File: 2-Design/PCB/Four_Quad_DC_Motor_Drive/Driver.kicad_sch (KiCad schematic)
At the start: 0 parts

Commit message: Changed the driver schematic, and added some schematic symbols
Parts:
- added C? (x3): 0.1uF, symbol Device:C_Polarized_Small_US
- added Q1, Q2, Q3, Q4: SPW47N60, symbol Device:Q_NMOS_GDS
- added U? (x4): HCPL-3120, Package_DIP:DIP-8_W7.62mm, symbol Driver_FET:HCPL-3120
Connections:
- new net: Q3.1 (G), U?.6 (VO), U?.7 (VO)
- new net: Q1.1 (G), U?.6 (VO), U?.7 (VO)
- new net: Q2.1 (G), U?.6 (VO), U?.7 (VO)
- new net: Q4.1 (G), U?.6 (VO), U?.7 (VO)
- new net +12V: C?.1, C?.1, C?.1, U?.8 (VCC), U?.8 (VCC), U?.8 (VCC), U?.8 (VCC)
- new net HVDC+: Q1.2 (D), Q3.2 (D)
- new net HVDC-: C?.2, Q2.3 (S), Q4.3 (S), U?.5 (VEE), U?.5 (VEE)
- new net MOTOR+: C?.2, Q1.3 (S), Q2.2 (D), U?.5 (VEE)
- new net MOTOR-: C?.2, Q3.3 (S), Q4.2 (D), U?.5 (VEE)

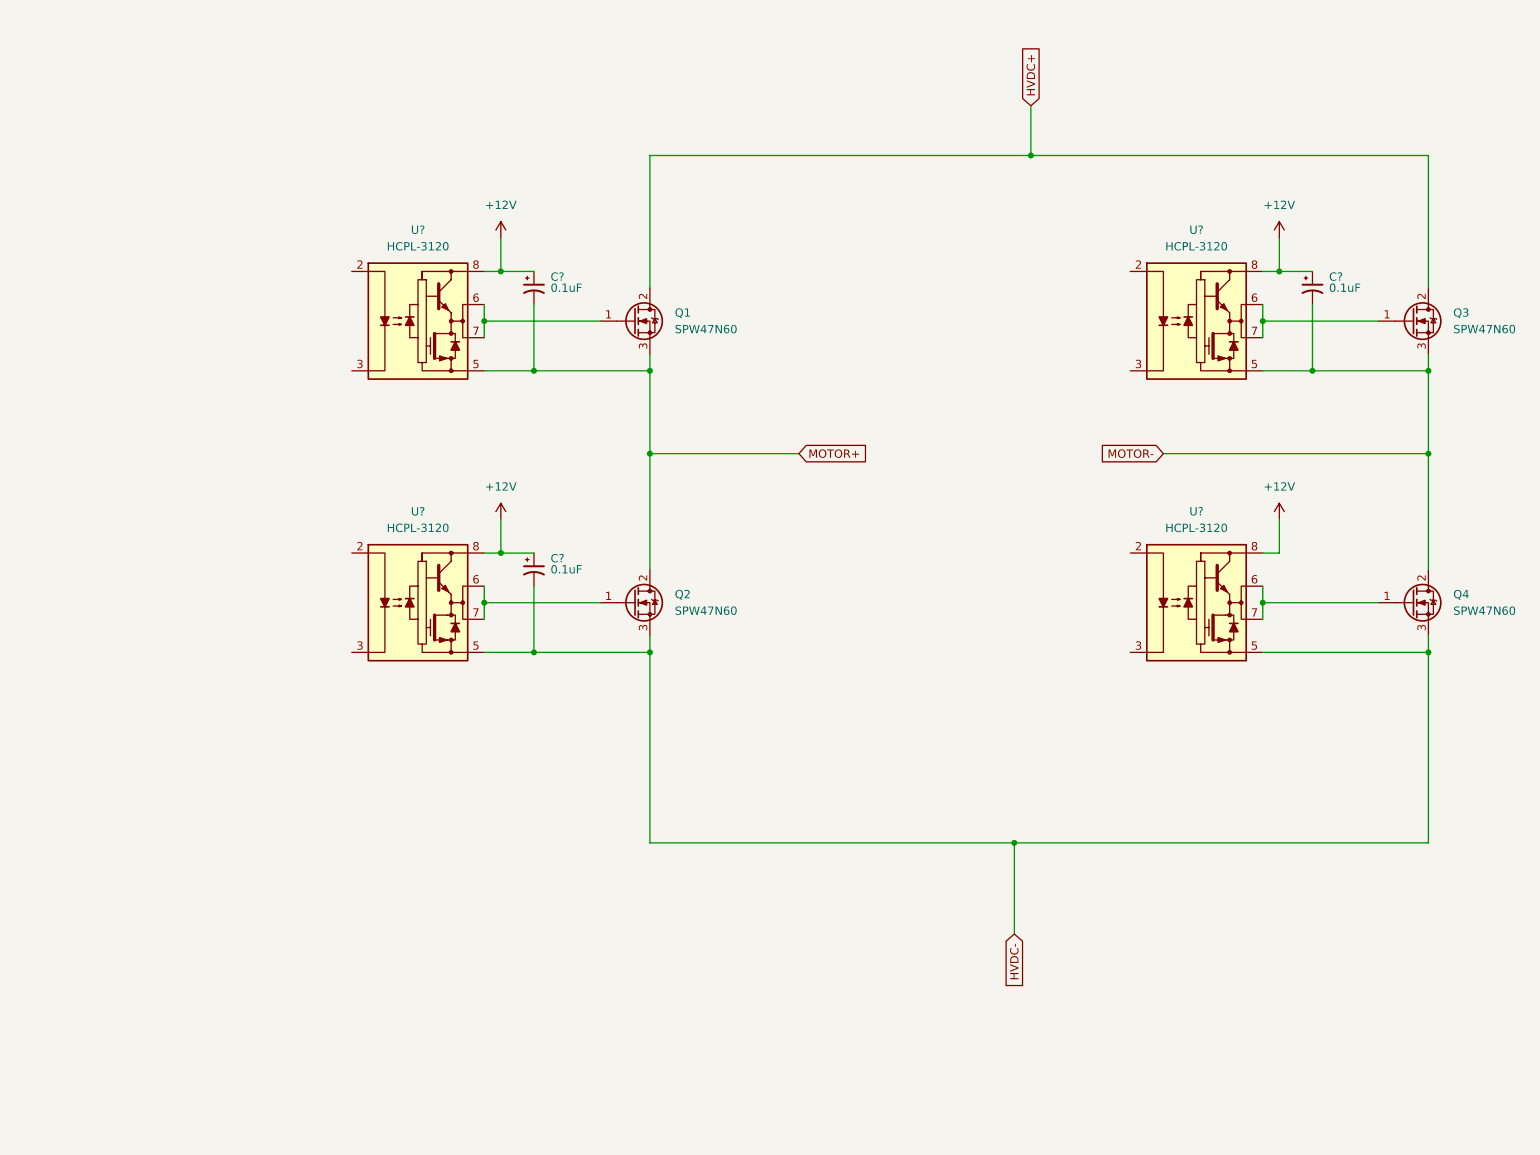
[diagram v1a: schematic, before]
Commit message: Added the gate driver schematics and converter schematics
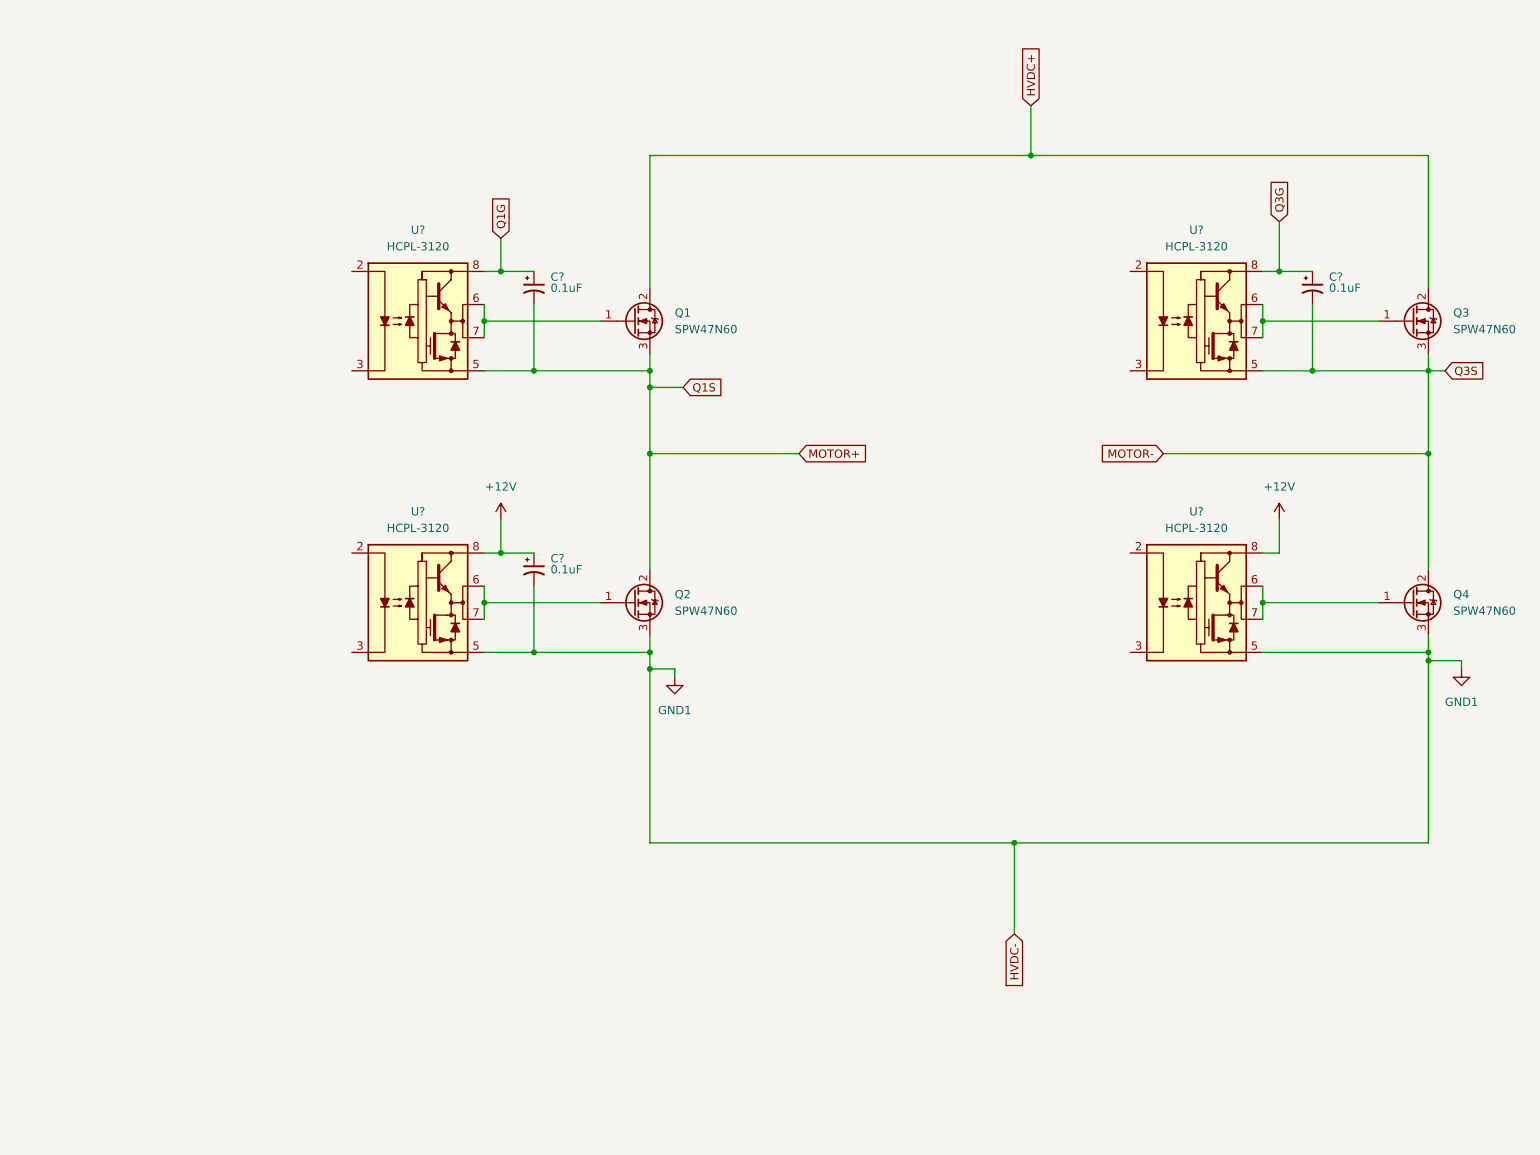
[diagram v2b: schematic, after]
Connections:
- net +12V: no longer C?.1, C?.1, U?.8 (VCC), U?.8 (VCC)
- net HVDC- renamed GND1
- new net Q1G: C?.1, U?.8 (VCC)
- new net Q3G: C?.1, U?.8 (VCC)
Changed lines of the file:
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@@
   (junction (at 121.92 111.76) (diameter 0) (color 0 0 0 0)
   )
+  (junction (at 241.3 113.03) (diameter 0) (color 0 0 0 0)
+  )
   (junction (at 99.06 53.34) (diameter 0) (color 0 0 0 0)
   )
@@
   (junction (at 96.52 104.14) (diameter 0) (color 0 0 0 0)
   )
+  (junction (at 121.92 114.3) (diameter 0) (color 0 0 0 0)
+  )
   (junction (at 121.92 81.28) (diameter 0) (color 0 0 0 0)
   )
@@
   (junction (at 241.3 68.58) (diameter 0) (color 0 0 0 0)
   )
+  (junction (at 121.92 71.12) (diameter 0) (color 0 0 0 0)
+  )
   (junction (at 121.92 68.58) (diameter 0) (color 0 0 0 0)
   )
@@
     (stroke (width 0) (type default) (color 0 0 0 0))
   )
+  (wire (pts (xy 121.92 71.12) (xy 127 71.12))
+    (stroke (width 0) (type default) (color 0 0 0 0))
+  )
+  (wire (pts (xy 218.44 45.72) (xy 218.44 53.34))
+    (stroke (width 0) (type default) (color 0 0 0 0))
+  )
+  (wire (pts (xy 125.73 114.3) (xy 125.73 115.57))
+    (stroke (width 0) (type default) (color 0 0 0 0))
+  )
   (wire (pts (xy 177.8 140.97) (xy 241.3 140.97))
     (stroke (width 0) (type default) (color 0 0 0 0))
@@
     (stroke (width 0) (type default) (color 0 0 0 0))
   )
+  (wire (pts (xy 241.3 68.58) (xy 243.84 68.58))
+    (stroke (width 0) (type default) (color 0 0 0 0))
+  )
   (wire (pts (xy 104.14 68.58) (xy 121.92 68.58))
     (stroke (width 0) (type default) (color 0 0 0 0))
@@
     (stroke (width 0) (type default) (color 0 0 0 0))
   )
-  (wire (pts (xy 121.92 111.76) (xy 121.92 140.97))
+  (wire (pts (xy 121.92 111.76) (xy 121.92 114.3))
     (stroke (width 0) (type default) (color 0 0 0 0))
   )
@@
     (stroke (width 0) (type default) (color 0 0 0 0))
   )
+  (wire (pts (xy 121.92 114.3) (xy 121.92 140.97))
+    (stroke (width 0) (type default) (color 0 0 0 0))
+  )
   (wire (pts (xy 215.9 96.52) (xy 218.44 96.52))
     (stroke (width 0) (type default) (color 0 0 0 0))
@@
     (stroke (width 0) (type default) (color 0 0 0 0))
   )
-  (wire (pts (xy 241.3 140.97) (xy 241.3 111.76))
+  (wire (pts (xy 241.3 140.97) (xy 241.3 113.03))
     (stroke (width 0) (type default) (color 0 0 0 0))
   )
@@
     (stroke (width 0) (type default) (color 0 0 0 0))
   )
-  (wire (pts (xy 121.92 68.58) (xy 121.92 81.28))
+  (wire (pts (xy 121.92 68.58) (xy 121.92 71.12))
     (stroke (width 0) (type default) (color 0 0 0 0))
   )
@@
     (stroke (width 0) (type default) (color 0 0 0 0))
   )
+  (wire (pts (xy 121.92 71.12) (xy 121.92 81.28))
+    (stroke (width 0) (type default) (color 0 0 0 0))
+  )
   (wire (pts (xy 104.14 111.76) (xy 121.92 111.76))
     (stroke (width 0) (type default) (color 0 0 0 0))
@@
     (stroke (width 0) (type default) (color 0 0 0 0))
   )
+  (wire (pts (xy 241.3 113.03) (xy 246.38 113.03))
+    (stroke (width 0) (type default) (color 0 0 0 0))
+  )
+  (wire (pts (xy 241.3 113.03) (xy 241.3 111.76))
+    (stroke (width 0) (type default) (color 0 0 0 0))
+  )
+  (wire (pts (xy 121.92 114.3) (xy 125.73 114.3))
+    (stroke (width 0) (type default) (color 0 0 0 0))
+  )
   (wire (pts (xy 215.9 111.76) (xy 241.3 111.76))
     (stroke (width 0) (type default) (color 0 0 0 0))
@@
     (stroke (width 0) (type default) (color 0 0 0 0))
   )
+  (wire (pts (xy 246.38 114.3) (xy 246.38 113.03))
+    (stroke (width 0) (type default) (color 0 0 0 0))
+  )
   (wire (pts (xy 96.52 104.14) (xy 114.3 104.14))
     (stroke (width 0) (type default) (color 0 0 0 0))
@@
   )
   (wire (pts (xy 241.3 81.28) (xy 241.3 99.06))
-    (stroke (width 0) (type default) (color 0 0 0 0))
-  )
-  (wire (pts (xy 218.44 48.26) (xy 218.44 53.34))
     (stroke (width 0) (type default) (color 0 0 0 0))
   )
@@
     )
   )
+  (global_label "Q1G" (shape input) (at 99.06 48.26 90) (fields_autoplaced)
+    (effects (font (size 1.27 1.27)) (justify left))
+    (property "Intersheet References" "${INTERSHEET_REFS}" (id 0) (at 98.9806 42.0369 90)
+      (effects (font (size 1.27 1.27)) (justify left) hide)
+    )
+  )
+  (global_label "Q3S" (shape input) (at 243.84 68.58 0) (fields_autoplaced)
+    (effects (font (size 1.27 1.27)) (justify left))
+    (property "Intersheet References" "${INTERSHEET_REFS}" (id 0) (at 250.0026 68.5006 0)
+      (effects (font (size 1.27 1.27)) (justify left) hide)
+    )
+  )
+  (global_label "Q1S" (shape input) (at 127 71.12 0) (fields_autoplaced)
+    (effects (font (size 1.27 1.27)) (justify left))
+    (property "Intersheet References" "${INTERSHEET_REFS}" (id 0) (at 133.1626 71.0406 0)
+      (effects (font (size 1.27 1.27)) (justify left) hide)
+    )
+  )
   (global_label "MOTOR-" (shape input) (at 200.66 81.28 180) (fields_autoplaced)
     (effects (font (size 1.27 1.27)) (justify right))
@@
     )
   )
+  (global_label "Q3G" (shape input) (at 218.44 45.72 90) (fields_autoplaced)
+    (effects (font (size 1.27 1.27)) (justify left))
+    (property "Intersheet References" "${INTERSHEET_REFS}" (id 0) (at 218.3606 39.4969 90)
+      (effects (font (size 1.27 1.27)) (justify left) hide)
+    )
+  )
   (symbol (lib_id "Device:C_Polarized_Small_US") (at 104.14 99.06 0) (unit 1)
     (in_bom yes) (on_board yes)
@@
     (pin "2")
   )
-  (symbol (lib_id "power:+12V") (at 218.44 91.44 0) (unit 1)
-    (in_bom yes) (on_board yes)
-    (property "Reference" "#PWR?" (id 0) (at 218.44 95.25 0)
-      (effects (font (size 1.27 1.27)) hide)
-    )
-    (property "Value" "+12V" (id 1) (at 218.44 86.36 0))
-    (property "Footprint" "" (id 2) (at 218.44 91.44 0)
-      (effects (font (size 1.27 1.27)) hide)
-    )
-    (property "Datasheet" "" (id 3) (at 218.44 91.44 0)
+  (symbol (lib_id "power:+12V") (at 99.06 91.44 0) (unit 1)
+    (in_bom yes) (on_board yes) (fields_autoplaced)
+    (property "Reference" "#PWR?" (id 0) (at 99.06 95.25 0)
+      (effects (font (size 1.27 1.27)) hide)
+    )
+    (property "Value" "+12V" (id 1) (at 99.06 86.36 0))
+    (property "Footprint" "" (id 2) (at 99.06 91.44 0)
+      (effects (font (size 1.27 1.27)) hide)
+    )
+    (property "Datasheet" "" (id 3) (at 99.06 91.44 0)
       (effects (font (size 1.27 1.27)) hide)
     )
@@
     (pin "8")
   )
-  (symbol (lib_id "power:+12V") (at 218.44 48.26 0) (unit 1)
-    (in_bom yes) (on_board yes)
-    (property "Reference" "#PWR?" (id 0) (at 218.44 52.07 0)
-      (effects (font (size 1.27 1.27)) hide)
-    )
-    (property "Value" "+12V" (id 1) (at 218.44 43.18 0))
-    (property "Footprint" "" (id 2) (at 218.44 48.26 0)
-      (effects (font (size 1.27 1.27)) hide)
-    )
-    (property "Datasheet" "" (id 3) (at 218.44 48.26 0)
+  (symbol (lib_id "power:GND1") (at 246.38 114.3 0) (unit 1)
+    (in_bom yes) (on_board yes) (fields_autoplaced)
+    (property "Reference" "#PWR?" (id 0) (at 246.38 120.65 0)
+      (effects (font (size 1.27 1.27)) hide)
+    )
+    (property "Value" "GND1" (id 1) (at 246.38 119.38 0))
+    (property "Footprint" "" (id 2) (at 246.38 114.3 0)
+      (effects (font (size 1.27 1.27)) hide)
+    )
+    (property "Datasheet" "" (id 3) (at 246.38 114.3 0)
       (effects (font (size 1.27 1.27)) hide)
     )
@@
     (pin "8")
   )
+  (symbol (lib_id "power:+12V") (at 218.44 91.44 0) (unit 1)
+    (in_bom yes) (on_board yes) (fields_autoplaced)
+    (property "Reference" "#PWR?" (id 0) (at 218.44 95.25 0)
+      (effects (font (size 1.27 1.27)) hide)
+    )
+    (property "Value" "+12V" (id 1) (at 218.44 86.36 0))
+    (property "Footprint" "" (id 2) (at 218.44 91.44 0)
+      (effects (font (size 1.27 1.27)) hide)
+    )
+    (property "Datasheet" "" (id 3) (at 218.44 91.44 0)
+      (effects (font (size 1.27 1.27)) hide)
+    )
+    (pin "1")
+  )
   (symbol (lib_id "Device:Q_NMOS_GDS") (at 119.38 104.14 0) (unit 1)
     (in_bom yes) (on_board yes) (fields_autoplaced)
@@
     (pin "1")
     (pin "2")
-  )
-  (symbol (lib_id "power:+12V") (at 99.06 91.44 0) (unit 1)
-    (in_bom yes) (on_board yes)
-    (property "Reference" "#PWR?" (id 0) (at 99.06 95.25 0)
-      (effects (font (size 1.27 1.27)) hide)
-    )
-    (property "Value" "+12V" (id 1) (at 99.06 86.36 0))
-    (property "Footprint" "" (id 2) (at 99.06 91.44 0)
-      (effects (font (size 1.27 1.27)) hide)
-    )
-    (property "Datasheet" "" (id 3) (at 99.06 91.44 0)
-      (effects (font (size 1.27 1.27)) hide)
-    )
-    (pin "1")
   )
   (symbol (lib_id "Device:Q_NMOS_GDS") (at 119.38 60.96 0) (unit 1)
@@
     (pin "8")
   )
-  (symbol (lib_id "power:+12V") (at 99.06 48.26 0) (unit 1)
-    (in_bom yes) (on_board yes)
-    (property "Reference" "#PWR?" (id 0) (at 99.06 52.07 0)
-      (effects (font (size 1.27 1.27)) hide)
-    )
-    (property "Value" "+12V" (id 1) (at 99.06 43.18 0))
-    (property "Footprint" "" (id 2) (at 99.06 48.26 0)
-      (effects (font (size 1.27 1.27)) hide)
-    )
-    (property "Datasheet" "" (id 3) (at 99.06 48.26 0)
-      (effects (font (size 1.27 1.27)) hide)
-    )
+  (symbol (lib_id "power:GND1") (at 125.73 115.57 0) (unit 1)
+    (in_bom yes) (on_board yes) (fields_autoplaced)
+    (property "Reference" "#PWR?" (id 0) (at 125.73 121.92 0)
+      (effects (font (size 1.27 1.27)) hide)
+    )
+    (property "Value" "GND1" (id 1) (at 125.73 120.65 0))
+    (property "Footprint" "" (id 2) (at 125.73 115.57 0)
+      (effects (font (size 1.27 1.27)) hide)
+    )
+    (property "Datasheet" "" (id 3) (at 125.73 115.57 0)
+      (effects (font (size 1.27 1.27)) hide)
+    )

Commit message: Added the label and gate drive resistances
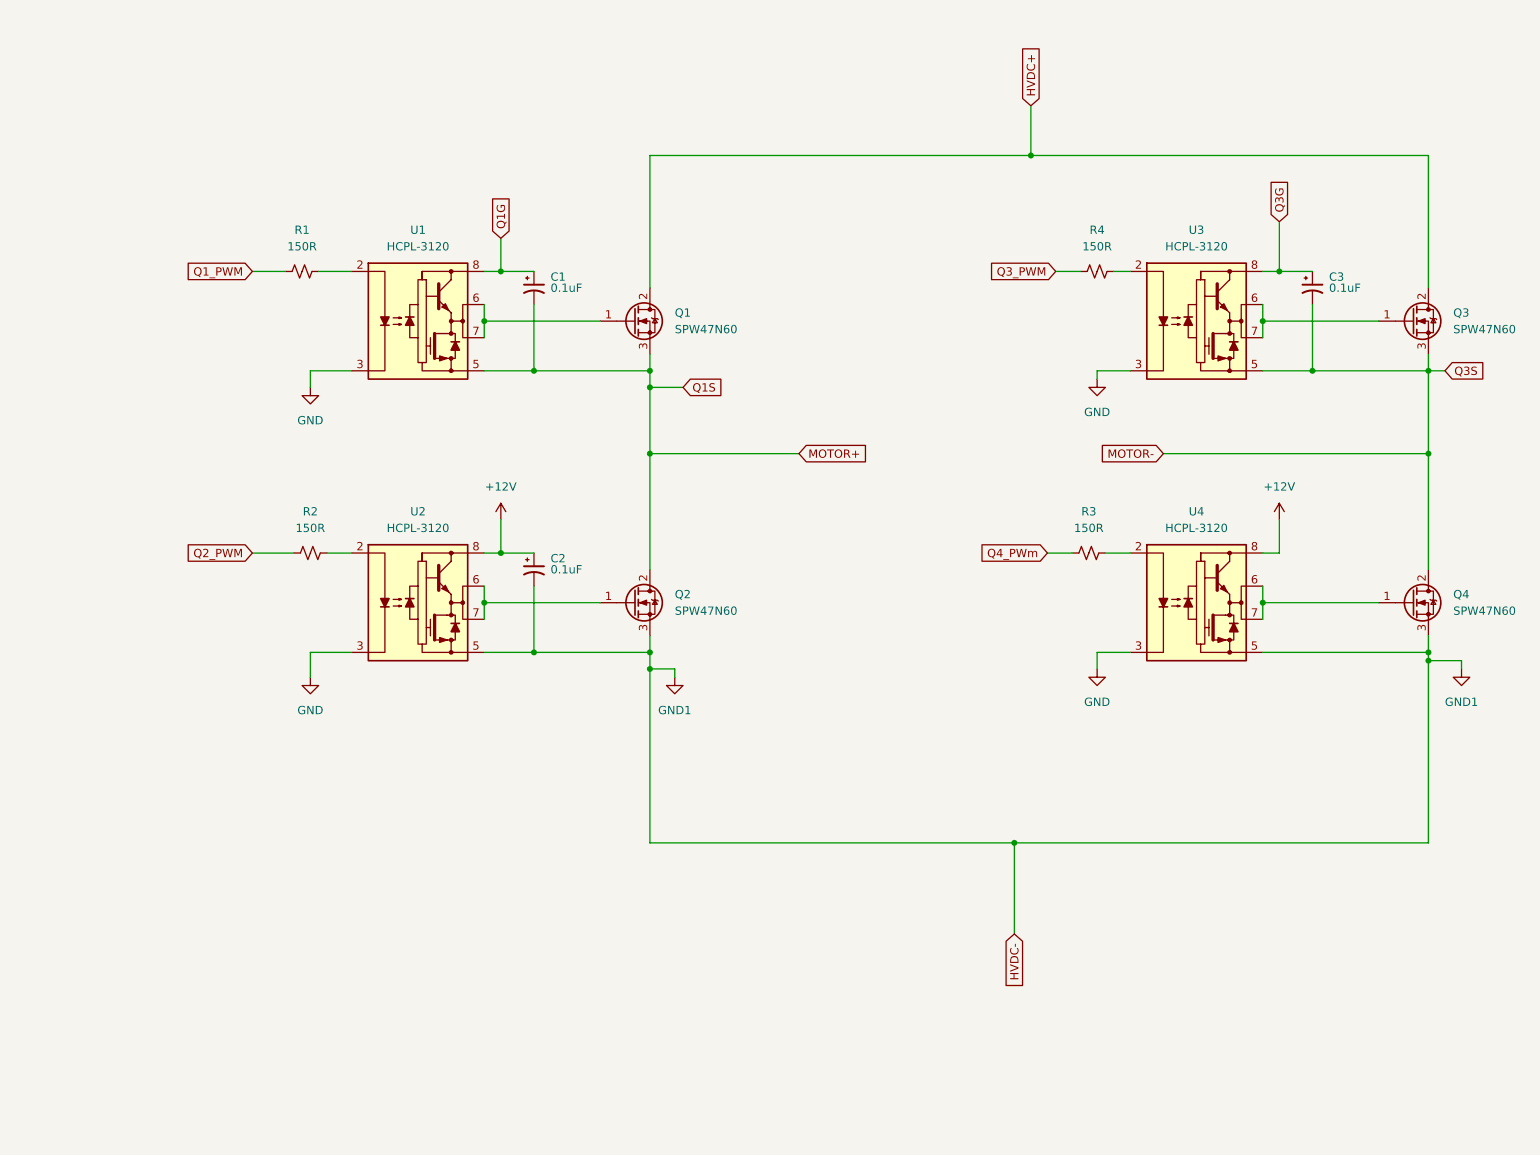
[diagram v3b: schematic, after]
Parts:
- added R1, R2, R3, R4: 150R, symbol Device:R_Small_US
- gave numbers to parts that had none: 7
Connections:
- net at U1.2 (A): now also R1.2
- net GND: now reaches U1.3 (C)
- net GND: now also U2.3 (C), U3.3 (C), U4.3 (C)
- net at U3.2 (A): now also R4.2
- net at U2.2 (A): now also R2.2
- net at U4.2 (A): now also R3.2
- new net Q1_PWM: R1.1
- new net Q2_PWM: R2.1
- new net Q3_PWM: R4.1
- new net Q4_PWm: R3.1
